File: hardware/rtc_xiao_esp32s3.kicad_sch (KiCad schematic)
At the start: 16 parts, among them J1 +5V, J2 GND, J3 SCL, J4 SDA, J5 CLKOUT, J6 NINT, U1 RV-3028-C8

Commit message: minor changes
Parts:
- U1: footprint Samacsys:RV3028C832768kHz1PPMTAQC -> Xiao RTC:RV3028C832768kHz1PPMTAQC
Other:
- note added: "RTS XIAO"
- note removed: "RTS for XIAO"
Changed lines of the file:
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@@
 		)
 	)
-	(text "RTS for XIAO"
+	(text "RTS XIAO"
 		(exclude_from_sim no)
-		(at 72.39 24.13 0)
+		(at 55.88 24.13 0)
 		(effects
 			(font
@@
 			)
 		)
-		(property "Footprint" "Samacsys:RV3028C832768kHz1PPMTAQC"
+		(property "Footprint" "Xiao RTC:RV3028C832768kHz1PPMTAQC"
 			(at 208.28 120.65 0)
 			(effects

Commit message: schematic update - useful notes added
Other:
- note added: "*1"
- note added: "*2"
- note added: "1* used battery delivers 1.55V so according to the documentation speed rate for I2C should be 100kHz while using the backup voltage source"
- note added: "2* battery size is SR66"
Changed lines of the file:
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@@
+		)
+	)
+	(text "*1"
+		(exclude_from_sim no)
+		(at 226.06 102.87 0)
+		(effects
+			(font
+				(size 1.27 1.27)
+			)
+		)
+	)
+	(text "2* battery size is SR66"
+		(exclude_from_sim no)
+		(at 203.2 138.43 0)
+		(effects
+			(font
+				(size 1.27 1.27)
+			)
+			(justify left)
+		)
+	)
+	(text "*2\n"
+		(exclude_from_sim no)
+		(at 226.06 105.41 0)
+		(effects
+			(font
+				(size 1.27 1.27)
+			)
+		)
+	)
+	(text "1* used battery delivers 1.55V \nso according to the documentation \nspeed rate for I2C should be 100kHz\nwhile using the backup voltage source "
+		(exclude_from_sim no)
+		(at 203.2 132.08 0)
+		(effects
+			(font
+				(size 1.27 1.27)
+			)
+			(justify left)
 		)
 	)

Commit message: nowe sockety 2.54mm
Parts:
- removed J1: +5V, TestPoint:TestPoint_THTPad_D1.5mm_Drill0.7mm, symbol Connector_Generic:Conn_01x01
- removed J2: GND, TestPoint:TestPoint_THTPad_D1.5mm_Drill0.7mm, symbol Connector_Generic:Conn_01x01
- removed J3: SCL, TestPoint:TestPoint_THTPad_D1.5mm_Drill0.7mm, symbol Connector_Generic:Conn_01x01
- removed J4: SDA, TestPoint:TestPoint_THTPad_D1.5mm_Drill0.7mm, symbol Connector_Generic:Conn_01x01
- removed J5: CLKOUT, TestPoint:TestPoint_THTPad_D1.5mm_Drill0.7mm, symbol Connector_Generic:Conn_01x01
- removed J6: NINT, TestPoint:TestPoint_THTPad_D1.5mm_Drill0.7mm, symbol Connector_Generic:Conn_01x01
- added J1: LEFT, Connector_PinHeader_2.54mm:PinHeader_1x07_P2.54mm_Vertical, symbol Connector:Conn_01x07_Socket
- added J2: RIGHT, Connector_PinHeader_2.54mm:PinHeader_1x07_P2.54mm_Vertical, symbol Connector:Conn_01x07_Socket
- BT1: Mouser Part Number 534-2998 -> (none); Mouser Price/Stock https://www.mouser.pl/ProductDetail/Keystone-Electronics/29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 -> (none)
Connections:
- net +5V: now also J1.7 (Pin_7)
- net CLKOUT: now also J2.4 (Pin_4)
- net GND: now also J1.1 (Pin_1), J1.2 (Pin_2), J1.3 (Pin_3), J1.4 (Pin_4), J1.5 (Pin_5), J1.6 (Pin_6), J2.1 (Pin_1), J2.5 (Pin_5), J2.6 (Pin_6)
- net NINT: now also J2.7 (Pin_7)
- net SCL: now also J2.2 (Pin_2)
- net SDA: now also J2.3 (Pin_3)
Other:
- note added: "SOCKETS"
- note removed: "PINS"
- moved on the sheet: C1, C2, JP1, R1, R2, R3, R4, R5, U1

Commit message: update to kicad10 & pcb dimension adjusted, changed pinout - 5V removed, 3v3 added
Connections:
- net GND: no longer J1.1 (Pin_1), J1.2 (Pin_2), J1.3 (Pin_3), J1.4 (Pin_4), J1.5 (Pin_5), J2.1 (Pin_1), J2.5 (Pin_5), J2.6 (Pin_6)
- net +5V renamed +3V3
- net +3V3: now also J1.5 (Pin_5); no longer J1.7 (Pin_7)
- no-connect marks 0 -> 8

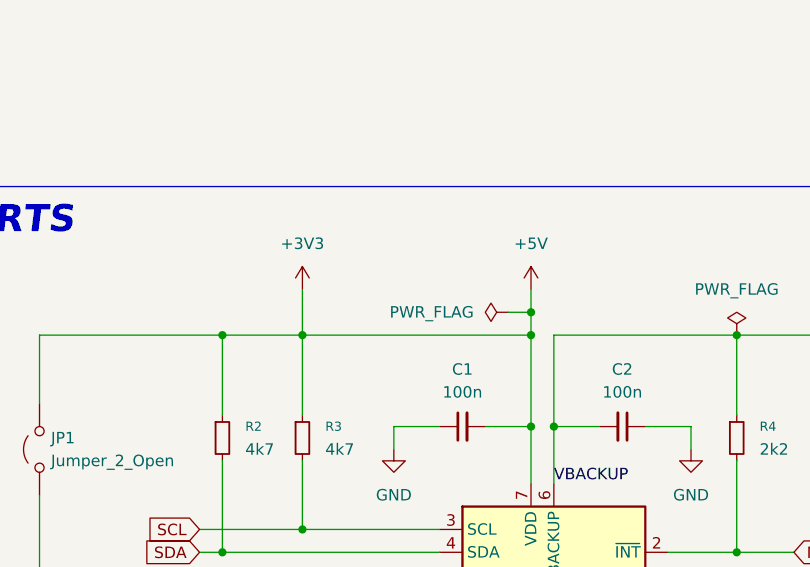
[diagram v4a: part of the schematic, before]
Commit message: 5V flag removed, battery holder links added, new gerber files and zip
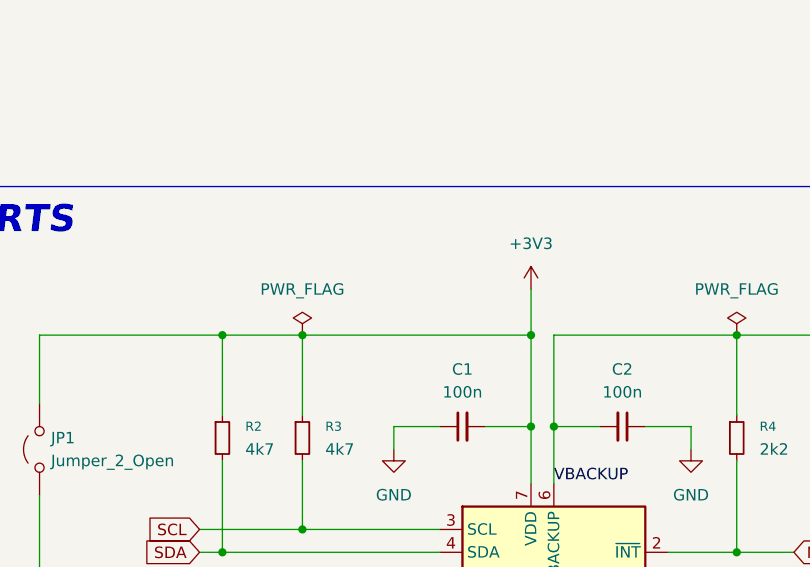
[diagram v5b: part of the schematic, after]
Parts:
- BT1: Mouser Part Number (none) -> 534-2998; Mouser Price/Stock (none) -> https://www.mouser.pl/ProductDetail/Keystone-Electronics/29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
